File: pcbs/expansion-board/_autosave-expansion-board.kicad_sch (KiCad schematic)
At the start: 75 parts, among them J1 Conn_01x02, J10 Conn_01x04, J11 Conn_01x04, J12 Raspberry_Pi_2_3, J13 Conn_01x04, J14 Conn_01x04, J15 Conn_01x06, J2 Conn_01x02, J3 Conn_02x03_Odd_Even, J4 Conn_02x03_Odd_Even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

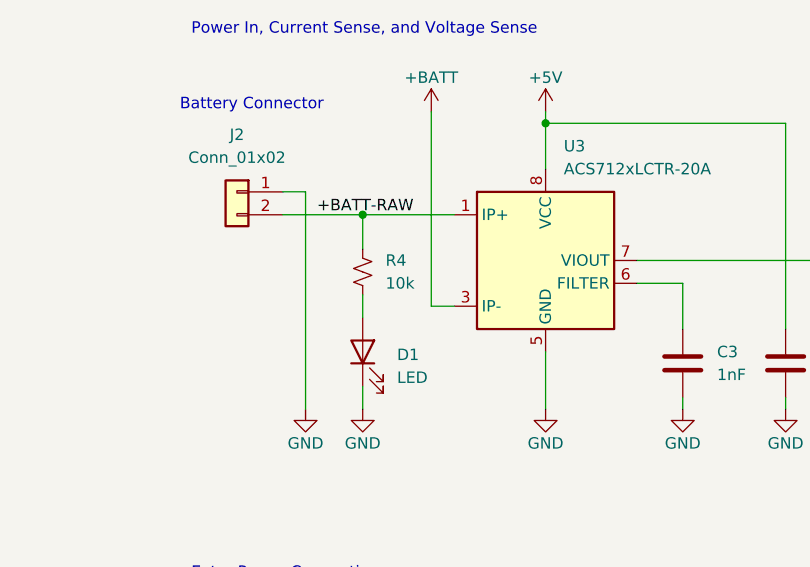
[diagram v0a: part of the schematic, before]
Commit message: minor expansion board fixes
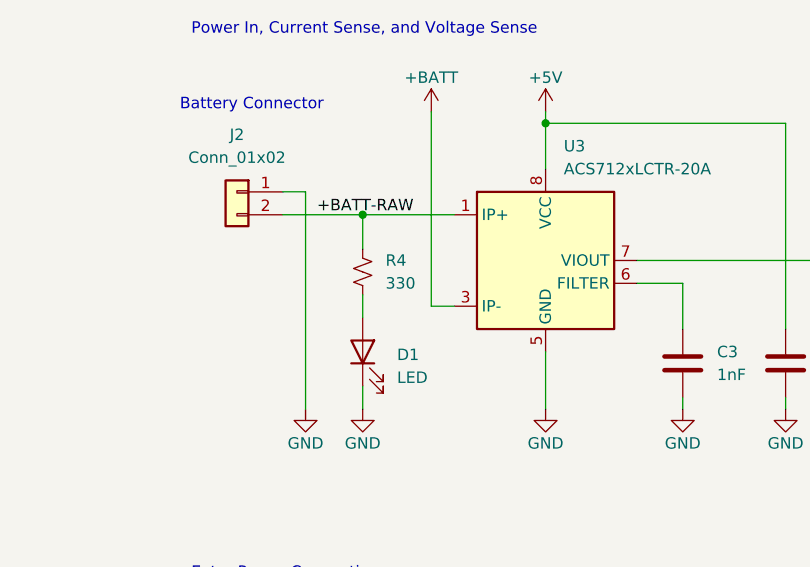
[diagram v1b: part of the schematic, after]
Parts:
- R4: value 10k -> 330
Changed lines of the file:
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@@
       (effects (font (size 1.27 1.27)) (justify right))
     )
-    (property "Value" "10k" (id 1) (at 132.08 77.4699 0)
+    (property "Value" "330" (id 1) (at 132.08 77.4699 0)
       (effects (font (size 1.27 1.27)) (justify right))
     )
@@
     )
     (path "/7348e0b5-e3a7-4428-af31-1dfd950cb78d"
-      (reference "R4") (unit 1) (value "10k") (footprint "Resistor_SMD:R_0805_2012Metric")
+      (reference "R4") (unit 1) (value "330") (footprint "Resistor_SMD:R_0805_2012Metric")
     )
     (path "/2f3f8c99-39c1-4e98-ab17-4a61187d76ba"
